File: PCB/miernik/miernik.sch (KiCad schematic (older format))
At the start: 40 parts, among them J1 Conn_01x01, J10 Conn_01x01, J11 Conn_01x01, J12 Conn_01x01, J2 Conn_01x01, J3 Conn_01x01, J4 Conn_01x01, J5 Conn_01x01, J6 Conn_01x01, J7 Conn_01x01, J8 Conn_01x01, J9 Conn_01x01, Q1 MMBTA42, Q2 MMBTA42, Q3 MMBTA42, SW1 SW_Push, SW2 SW_Push, SW3 SW_Push, U1 ATmega8-16PU, U2 3DIGIT-7SEGMENT, U3 A1101ELHL, Y1 Crystal

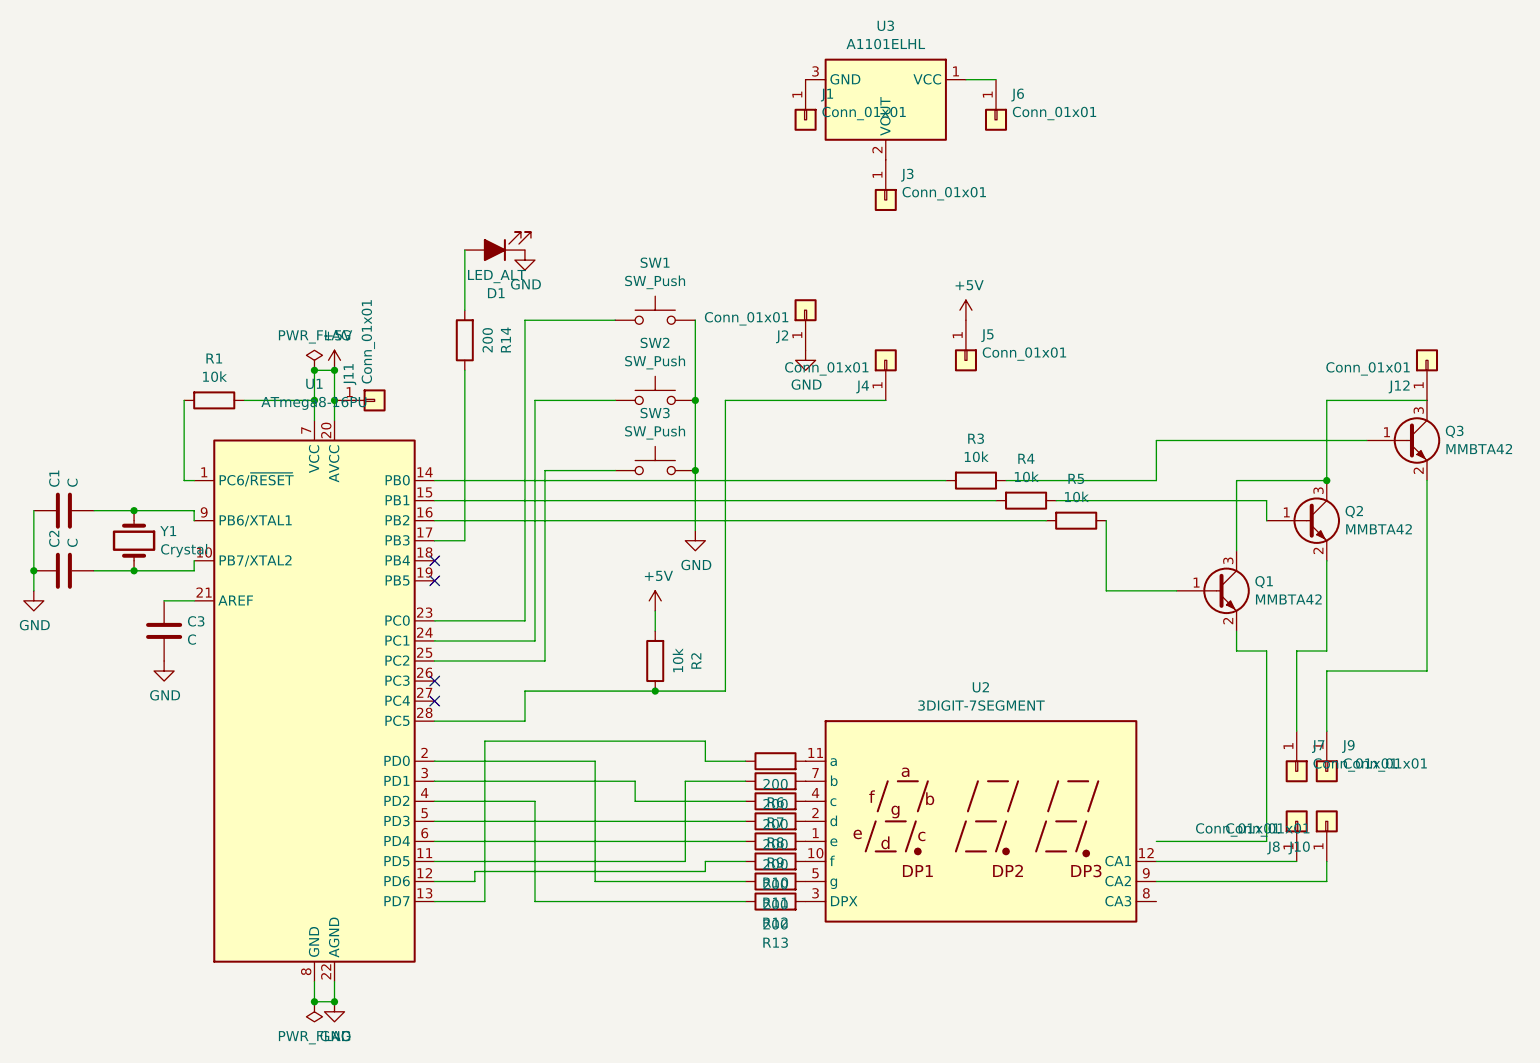
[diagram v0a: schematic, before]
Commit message: Add files via upload
Added temperature sensor, added some letters and names for modes, fixed problem with float in total distance.
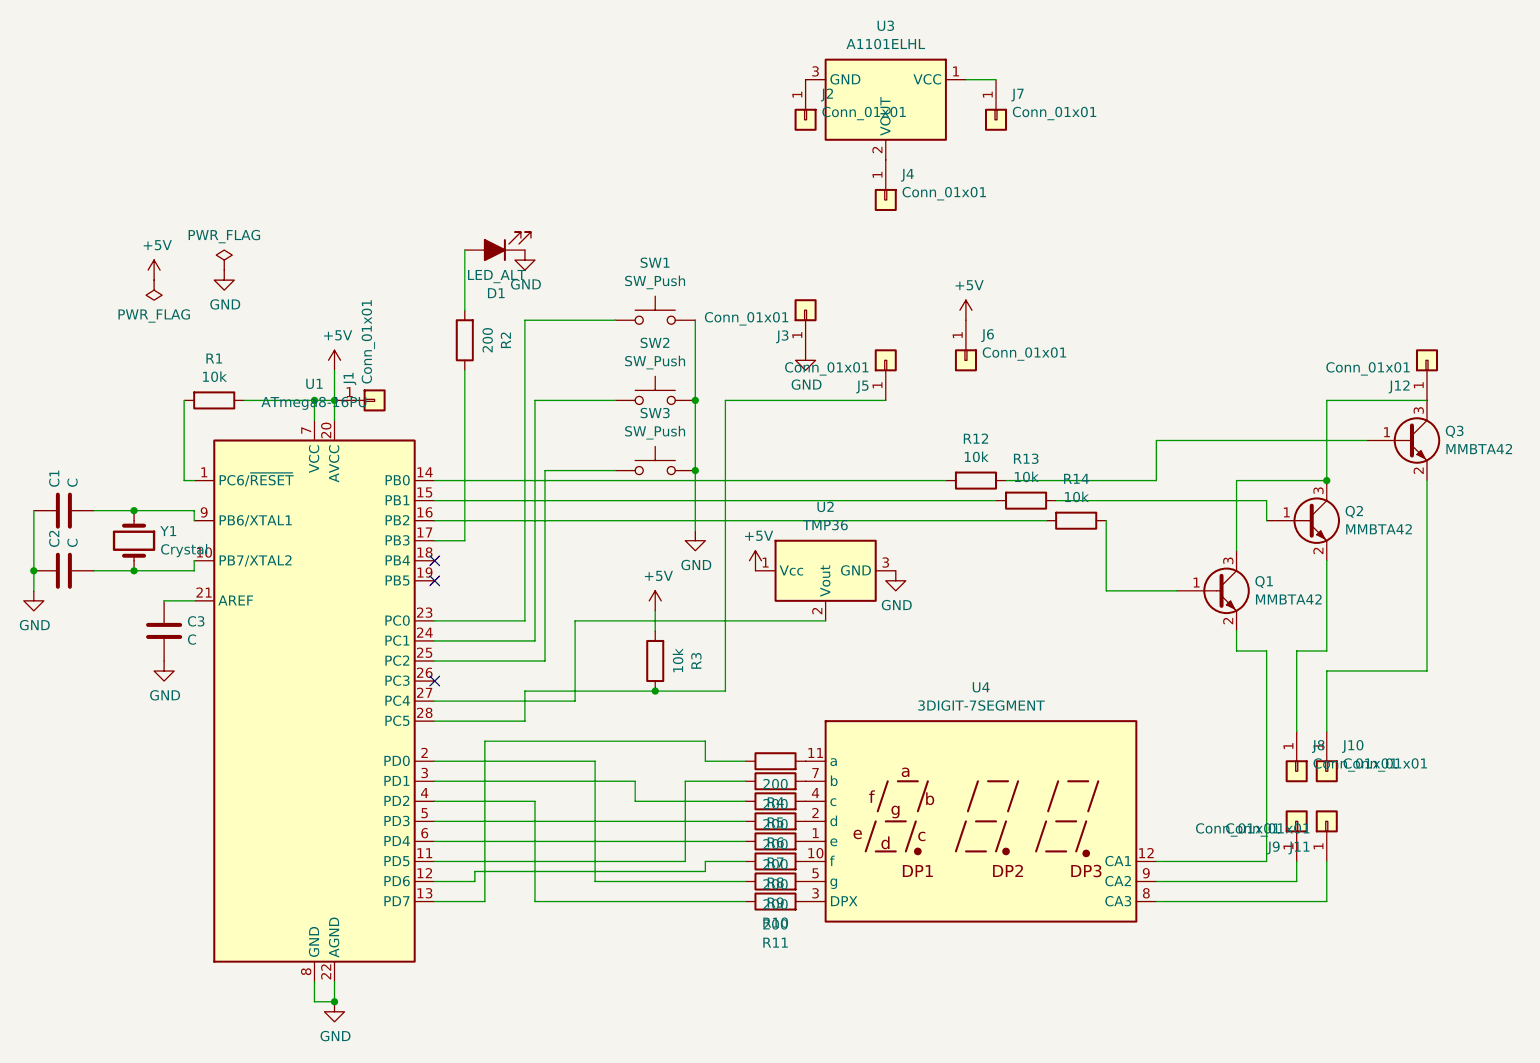
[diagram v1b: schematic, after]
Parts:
- added U2: TMP36, Package_TO_SOT_THT:TO-92, symbol Sensor_Temperature:TMP36
- renumbered J11 to J1, J9 to J10, J10 to J11, J1 to J2, J2 to J3, J3 to J4, J4 to J5, J5 to J6, J6 to J7, J7 to J8, J8 to J9, R12 to R10, R13 to R11, R3 to R12, R4 to R13, R5 to R14, R14 to R2, R2 to R3, R6 to R4, R7 to R5, R8 to R6, R9 to R7, R10 to R8, R11 to R9, U2 to U4
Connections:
- net +5V: now also U2.1 (Vcc)
- net GND: now also U2.3 (GND)
- net at U1.27 (PC4): now also U2.2 (Vout)
- net at Q1.2 (E): now also U4.12 (CA1)
- net at J9.1 (Pin_1): now also U4.9 (CA2); no longer U4.12 (CA1)
- net at U4.8 (CA3): now also J11.1 (Pin_1)
- no-connect marks 4 -> 3
